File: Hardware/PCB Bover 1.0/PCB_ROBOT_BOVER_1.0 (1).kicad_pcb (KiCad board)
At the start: 2 copper layers, 70 x 100 mm, 34 parts, among them J1 HC_SRO4, J10 KY_032, J2 HC_SRO4, J3 HC_SRO4, J4 HC_SRO4, J5 Alimentacion, J7 M1, J8 M2, J9 KY_032, U1 L298N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

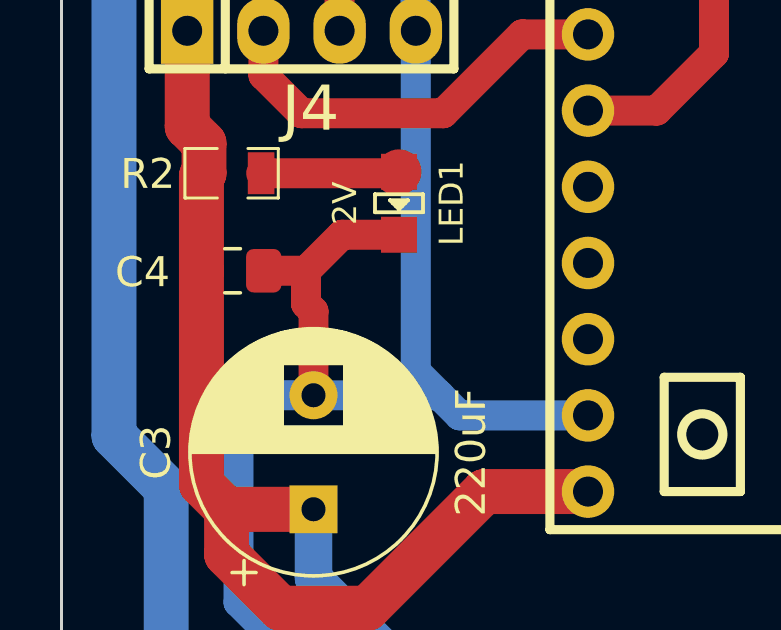
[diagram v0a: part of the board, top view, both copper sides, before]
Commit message: add the designs and PCB edit
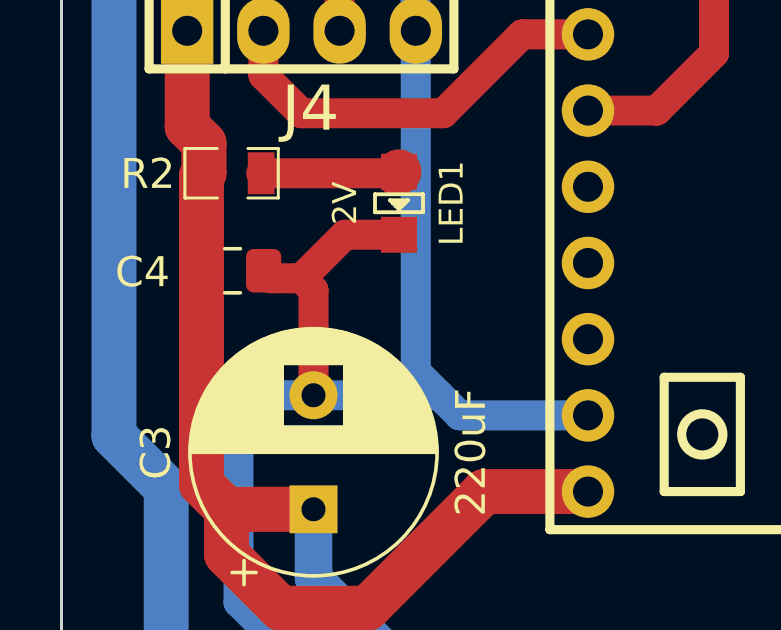
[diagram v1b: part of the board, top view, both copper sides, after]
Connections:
- C3 pad 2: GND -> Net-(C3-Pad2)
- C4 pad 1: GND -> Net-(C3-Pad2)
- LED1 pad 2: GND -> Net-(C3-Pad2)
- U2 pad 2: GND -> Net-(C3-Pad2)
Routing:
- net Net-(C3-Pad2): track 0.00 -> 9.28 mm
- net GND: track 290.7 -> 281.5 mm
